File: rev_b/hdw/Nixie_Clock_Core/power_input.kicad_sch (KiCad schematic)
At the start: 30 parts, among them J601 +12V IN, U601 TPS26600RHFT

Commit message: lots of rev B control board schematic progress
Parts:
- removed R601, R603: 100k, Resistors_SMD:R_0402, symbol Custom_Library:R_Custom
- removed R602, R605, R621: 10k, Resistors_SMD:R_0402, symbol Custom_Library:R_Custom
- removed R604, R615, R616, R617: 1k, Resistors_SMD:R_0402, symbol Custom_Library:R_Custom
- added R?: 200k, Resistors_SMD:R_0402, symbol Custom_Library:R_Custom
- added R?: 1.78k, Resistors_SMD:R_0402, symbol Custom_Library:R_Custom
- added R?: 10k, Resistors_SMD:R_0402, symbol Custom_Library:R_Custom
- C?: renamed from C603; value 100uF -> 47uF; Digi-Key PN 718-1102-1-ND -> 399-3905-1-ND; Voltage 16V -> 35V
- D?: renamed from D601; value 24V -> 48V; Digi-Key PN SMAJ24CALFCT-ND -> (none)
- J?: renamed from J601; value +12V IN -> +24V IN
- R?: renamed from R619; value 10k -> 1.6k; Digi-Key PN RMCF0402FT10K0CT-ND -> (none)
- renumbered C602 to C?, C601 to C?, R612 to R?, R611 to R?, R607 to R?, R614 to R?, R610 to R?, R618 to R?, R620 to R?, R606 to R?, R609 to R?, R608 to R?, R613 to R?, TP601 to TP?, TP602 to TP?, TP603 to TP?, U601 to U?
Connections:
- net +12V is gone; now on net +24V: C?.1, R?.2, R?.2, R?.2, R?.2, R?.2, TP?.1 (TP)
- net at C?.2, R?.2, R?.2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: now also R?.2
- net at U?.10 (UVLO): now also R?.1, R?.2
- net at U?.12 (OVP): now also R?.1, R?.2
- net +24V: now reaches R?.1
- net +12Vin renamed +24Vin
- net +24Vin: now also R?.1
- net POS12_PGOOD renamed POS24_PGOOD
- net POS12_SNS+ renamed POS24_SNS+
- net POS12_SNS- renamed POS24_SNS-
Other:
- note added: "UVLO threshold set to ~22VV OVLO threshold set to ~26V MODE set to Circuit Breaker with Auto-Retry Output Current Limit set to 1.2A Output ramp rate = 12.5V/ms"
- note removed: "CHANGE TO 24V BUS"
- note removed: "UVLO threshold set to 11.12V OVLO threshold set to 13.33V MODE set to Circuit Breaker with Auto-Retry Output Current Limit set to 1.2A Output ramp rate = 12.5V/ms"
- moved on the sheet: R?

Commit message: more rev b sch progress
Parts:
- added C? (x4): 10uF, symbol Custom Library:C_Custom
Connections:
- net +24V: now also C?.1, C?.1
- net +24Vin: now also C?.1, C?.1
- net GND: now also C?.2, C?.2, C?.2, C?.2
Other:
- moved on the sheet: C?, D?, J?, R?, TP?, U?

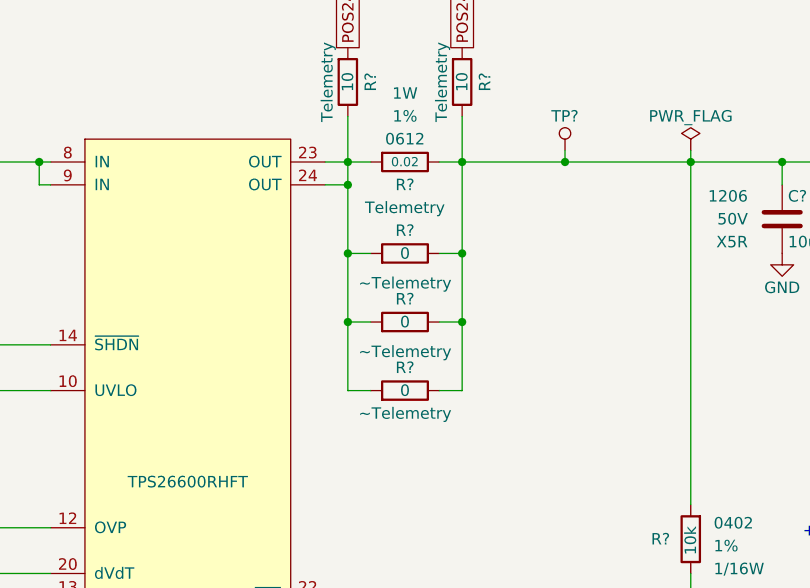
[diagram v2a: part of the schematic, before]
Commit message: more schematic progress, assigning signals to MCU"
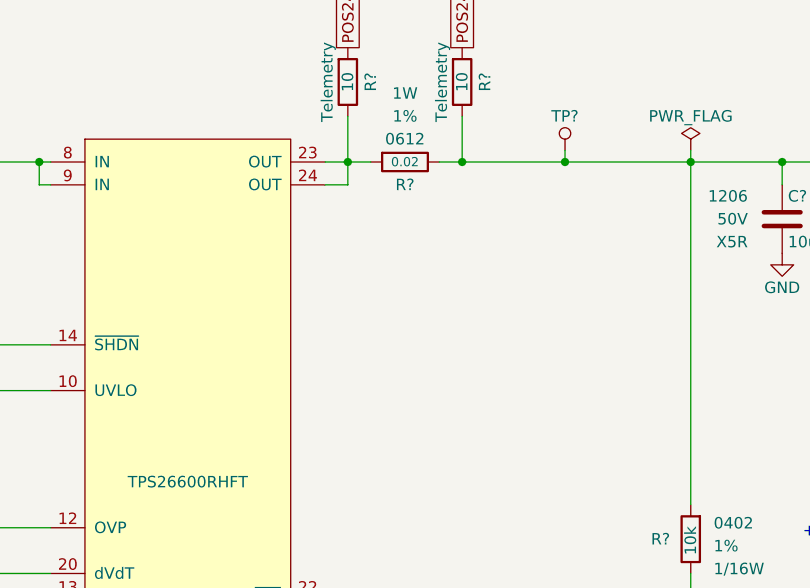
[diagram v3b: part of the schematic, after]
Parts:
- removed R? (x3): 0, Resistors_SMD:R_0402, symbol Custom_Library:R_Custom
- R?: Configuration Telemetry -> (none)

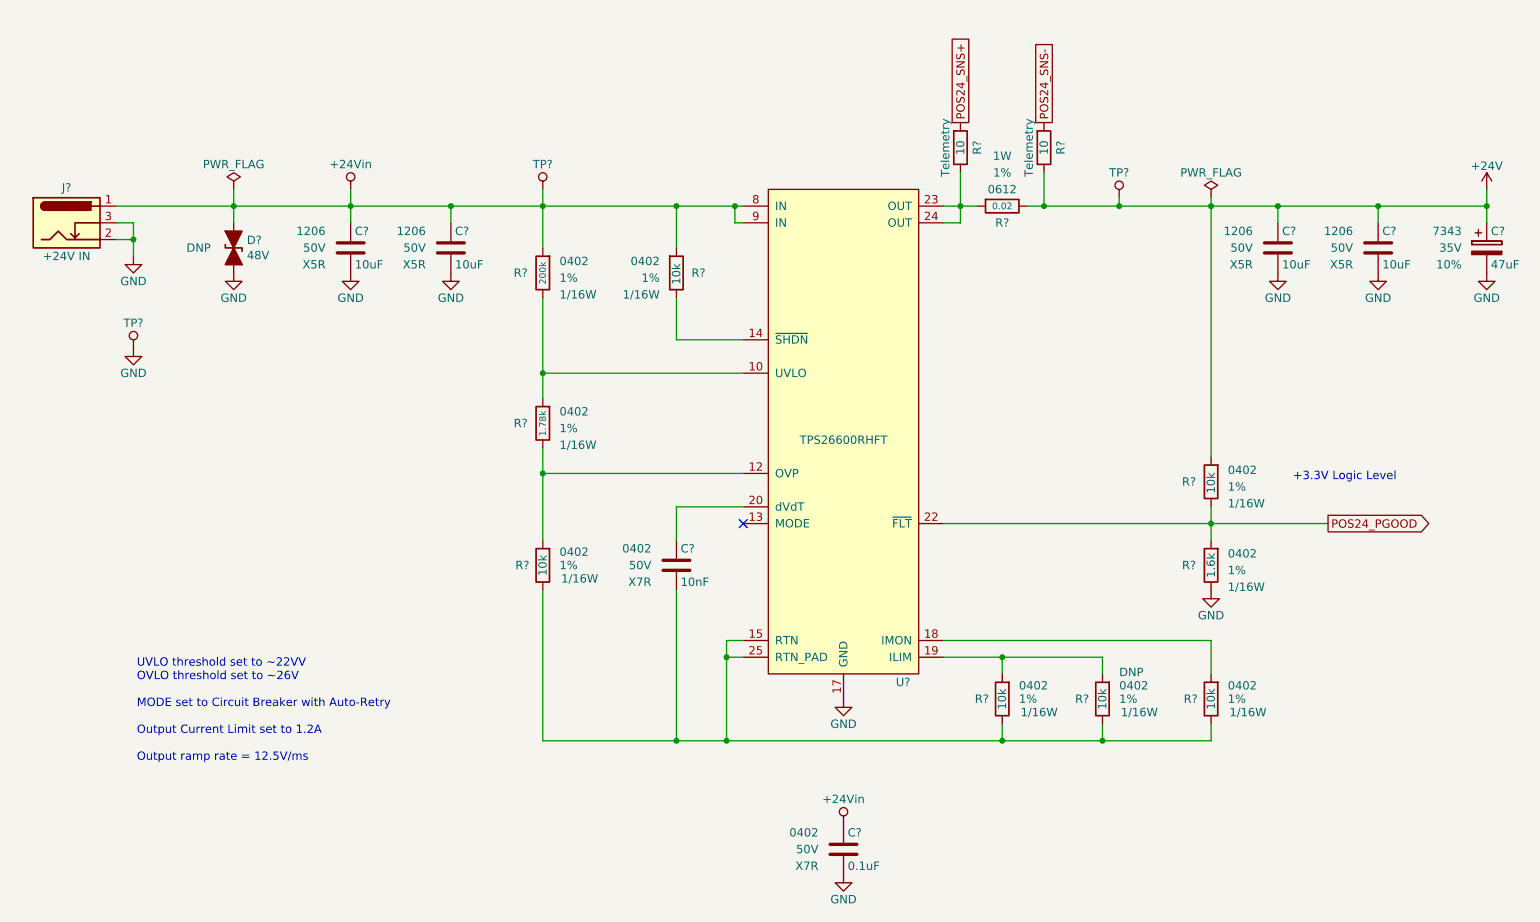
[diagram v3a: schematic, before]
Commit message: updated footprints, ran some DRC
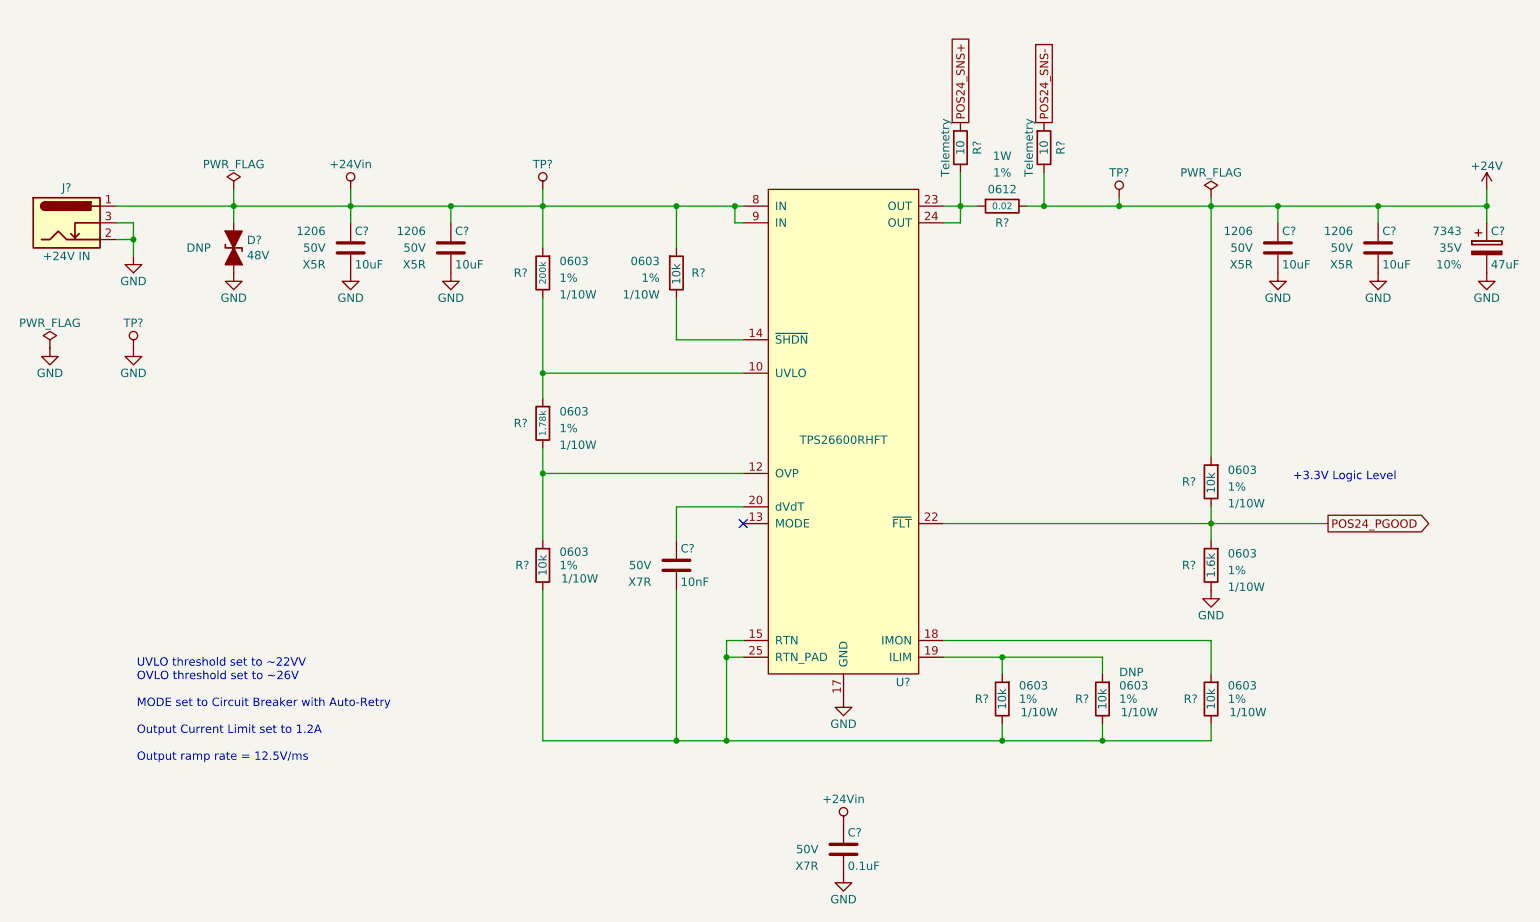
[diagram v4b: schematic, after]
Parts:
- C? (x4): footprint (none) -> Capacitors_SMD:C_1206; Digi-Key PN 1276-6736-1-ND -> (none)
- C?: footprint Capacitors_SMD:C_0402 -> Capacitors_SMD:C_0603; Digi-Key PN 490-10698-1-ND -> (none); display_footprint 0402 -> (none)
- C?: footprint Capacitors_SMD:C_0402 -> Capacitors_SMD:C_0603; Digi-Key PN 399-3066-1-ND -> (none); display_footprint 0402 -> (none)
- C?: footprint Capacitors_Tantalum_SMD:CP_Tantalum_Case-X_EIA-7343-43_Reflow -> Capacitor_Tantalum_SMD:CP_EIA-7343-43_Kemet-X; Digi-Key PN 399-3905-1-ND -> (none)
- R? (x6): footprint Resistors_SMD:R_0402 -> Resistors_SMD:R_0603; Digi-Key PN RMCF0402FT10K0CT-ND -> (none); Wattage 1/16W -> 1/10W; display_footprint 0402 -> 0603
- R? (x2): footprint Resistors_SMD:R_0402 -> Resistors_SMD:R_0603; Digi-Key PN RMCF0402FT10R0CT-ND -> (none); Wattage 1/16W -> 1/10W; display_footprint 0402 -> 0603
- R? (x3): footprint Resistors_SMD:R_0402 -> Resistors_SMD:R_0603; Wattage 1/16W -> 1/10W; display_footprint 0402 -> 0603
- TP?: footprint Pin_Headers:Pin_Header_Angled_1x01_Pitch2.54mm -> Connector_PinHeader_2.54mm:PinHeader_1x01_P2.54mm_Horizontal

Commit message: hid all passive refdes on core PCB
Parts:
- C? (x4): Digi-Key PN (none) -> 1276-6767-1-ND
- C?: Digi-Key PN (none) -> 1276-1935-1-ND; display_footprint (none) -> 0603
- C?: Digi-Key PN (none) -> 1276-1009-1-ND; display_footprint (none) -> 0603
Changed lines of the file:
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@@
       (effects (font (size 1.27 1.27)) (justify right))
     )
-    (property "Digi-Key PN" "" (at 98.425 50.8 0)
+    (property "Digi-Key PN" "1276-6767-1-ND" (at 98.425 50.8 0)
       (effects (font (size 1.524 1.524)) hide)
     )
@@
       (effects (font (size 1.27 1.27)) (justify right))
     )
-    (property "Digi-Key PN" "" (at 224.155 50.8 0)
+    (property "Digi-Key PN" "1276-6767-1-ND" (at 224.155 50.8 0)
       (effects (font (size 1.524 1.524)) hide)
     )
@@
       (effects (font (size 1.27 1.27)) hide)
     )
-    (property "display_footprint" "" (at 143.51 152.4 0)
+    (property "display_footprint" "0603" (at 143.51 152.4 0)
       (effects (font (size 1.27 1.27)) (justify right))
     )
@@
       (effects (font (size 1.27 1.27)) (justify right))
     )
-    (property "Digi-Key PN" "" (at 158.115 142.24 0)
+    (property "Digi-Key PN" "1276-1935-1-ND" (at 158.115 142.24 0)
       (effects (font (size 1.524 1.524)) hide)
     )
@@
       (effects (font (size 1.27 1.27)) hide)
     )
-    (property "display_footprint" "" (at 118.11 109.22 0)
+    (property "display_footprint" "0603" (at 118.11 109.22 0)
       (effects (font (size 1.27 1.27)) (justify right))
     )
@@
       (effects (font (size 1.27 1.27)) (justify right))
     )
-    (property "Digi-Key PN" "" (at 132.715 99.06 0)
+    (property "Digi-Key PN" "1276-1009-1-ND" (at 132.715 99.06 0)
       (effects (font (size 1.524 1.524)) hide)
     )
@@
       (effects (font (size 1.27 1.27)) (justify right))
     )
-    (property "Digi-Key PN" "" (at 83.185 50.8 0)
+    (property "Digi-Key PN" "1276-6767-1-ND" (at 83.185 50.8 0)
       (effects (font (size 1.524 1.524)) hide)
     )
@@
       (effects (font (size 1.27 1.27)) (justify right))
     )
-    (property "Digi-Key PN" "" (at 239.395 50.8 0)
+    (property "Digi-Key PN" "1276-6767-1-ND" (at 239.395 50.8 0)
       (effects (font (size 1.524 1.524)) hide)
     )

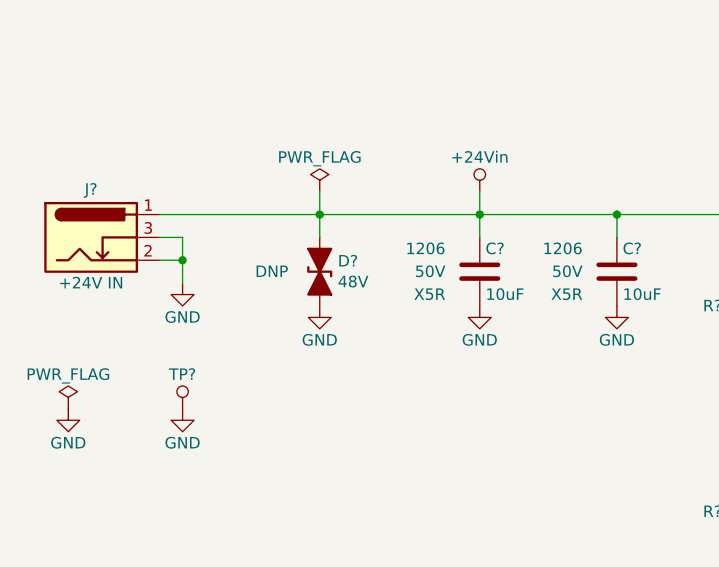
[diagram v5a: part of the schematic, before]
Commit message: arranged USB components on PCB, added USB isolator Bypass
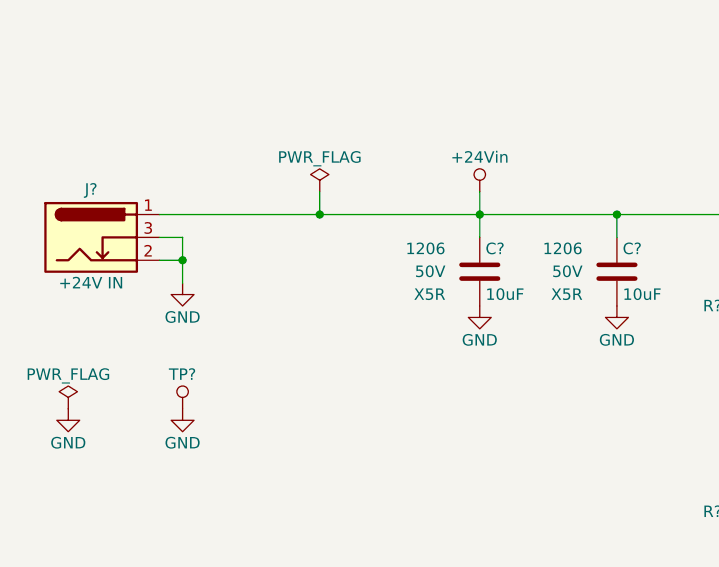
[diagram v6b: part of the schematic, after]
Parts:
- removed D?: 48V, Diodes_SMD:D_SMA, symbol Device:D_TVS_ALT
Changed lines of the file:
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@@
-    (stroke (width 0) (type default))
-  )
-  (wire (pts (xy 54.61 59.69) (xy 54.61 57.15))
     (stroke (width 0) (type default))
   )
@@
         (path "/16fdce21-b570-4d81-a458-e8839d611806/033277b9-3b61-4d88-889d-97b223ca74c5"
           (reference "#PWR0201") (unit 1)
-        )
-      )
-    )
-  )
-  (symbol (lib_id "power:GND") (at 54.61 67.31 0) (unit 1)
-    (in_bom yes) (on_board yes) (dnp no)
-    (property "Reference" "#PWR?" (at 54.61 73.66 0)
-      (effects (font (size 1.27 1.27)) hide)
-    )
-    (property "Value" "GND" (at 54.61 71.12 0)
-      (effects (font (size 1.27 1.27)))
-    )
-    (property "Footprint" "" (at 54.61 67.31 0)
-      (effects (font (size 1.27 1.27)) hide)
-    )
-    (property "Datasheet" "" (at 54.61 67.31 0)
-      (effects (font (size 1.27 1.27)) hide)
-    )
-    (pin "1")
-    (instances
-      (project "Nixie_Clock_Core"
-        (path "/16fdce21-b570-4d81-a458-e8839d611806/0b6dccc1-0a92-424d-9916-2441ea7dc052"
-          (reference "#PWR?") (unit 1)
-        )
-        (path "/16fdce21-b570-4d81-a458-e8839d611806/033277b9-3b61-4d88-889d-97b223ca74c5"
-          (reference "#PWR0208") (unit 1)
-        )
-      )
-      (project "LED_Panel_Controller"
-        (path "/22e05ee1-b227-4be7-9418-94433f274720/00000000-0000-0000-0000-00005f581b41"
-          (reference "#PWR?") (unit 1)
         )
       )
@@
         )
       )
-    )
-  )
-  (symbol (lib_id "Device:D_TVS_ALT") (at 54.61 63.5 270) (unit 1)
-    (in_bom yes) (on_board yes) (dnp no)
-    (property "Reference" "D?" (at 56.6166 62.3316 90)
-      (effects (font (size 1.27 1.27)) (justify left))
-    )
-    (property "Value" "48V" (at 56.6166 64.643 90)
-      (effects (font (size 1.27 1.27)) (justify left))
-    )
-    (property "Footprint" "Diodes_SMD:D_SMA" (at 54.61 63.5 0)
-      (effects (font (size 1.27 1.27)) hide)
-    )
-    (property "Datasheet" "~" (at 54.61 63.5 0)
-      (effects (font (size 1.27 1.27)) hide)
-    )
-    (property "Digi-Key PN" "" (at 54.61 63.5 0)
-      (effects (font (size 1.27 1.27)) hide)
-    )
-    (property "Configuration" "DNP" (at 49.276 63.5 90)
-      (effects (font (size 1.27 1.27)))
-    )
-    (pin "1")
-    (pin "2")
-    (instances
-      (project "Nixie_Clock_Core"
-        (path "/16fdce21-b570-4d81-a458-e8839d611806/0b6dccc1-0a92-424d-9916-2441ea7dc052"
-          (reference "D?") (unit 1)
-        )
-        (path "/16fdce21-b570-4d81-a458-e8839d611806/033277b9-3b61-4d88-889d-97b223ca74c5"
-          (reference "D201") (unit 1)
-        )
-      )
-      (project "LED_Panel_Controller"
-        (path "/22e05ee1-b227-4be7-9418-94433f274720/00000000-0000-0000-0000-00005f581b41"
-          (reference "D?") (unit 1)
-        )
-      )
